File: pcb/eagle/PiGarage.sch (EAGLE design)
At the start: 19 parts, among them J1 JST_2PIN_HEADER, J2 JST_2PIN_HEADER, J3 JST_2PIN_HEADER, J4 RPI-GPIO-20X2, K1 G5LE, T1 NUD3105

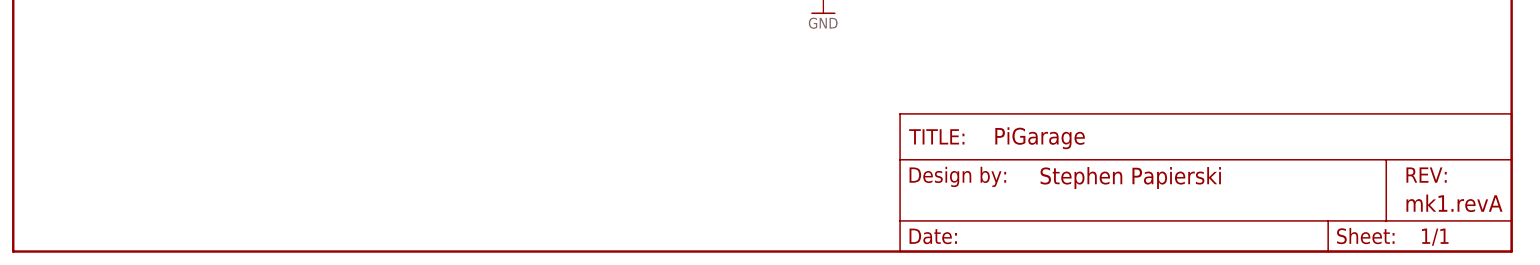
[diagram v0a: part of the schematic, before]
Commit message: Fixed relay NC/NO pin swap issue, bumped board rev to mk1.revB
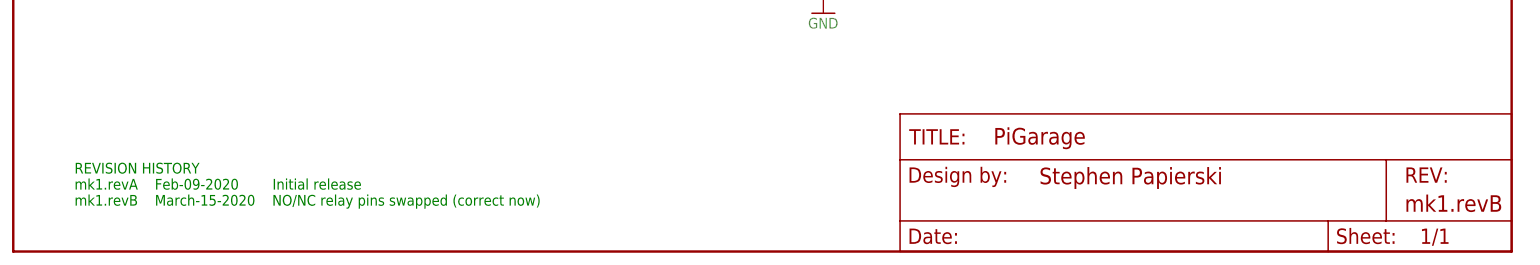
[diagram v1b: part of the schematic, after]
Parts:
- FRAME1: REV mk1.revA -> mk1.revB
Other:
- note added: "REVISION HISTORY mk1.revA Feb-09-2020 Initial release mk1.revB March-15-2020 NO/NC relay pins swapped (correct now)"
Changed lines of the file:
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@@
 <?xml version="1.0" encoding="utf-8"?>
 <!DOCTYPE eagle SYSTEM "eagle.dtd">
-<eagle version="9.2.0">
+<eagle version="9.5.2">
 <drawing>
 <settings>
-<setting alwaysvectorfont="yes"/>
+<setting alwaysvectorfont="no"/>
 <setting verticaltext="up"/>
 </settings>
@@
 <part name="FRAME1" library="eagle_stephen_v1.1" deviceset="FRAME-LETTER" device="NO_PACKAGE">
 <attribute name="DESIGNER" value="Stephen Papierski"/>
-<attribute name="REV" value="mk1.revA"/>
+<attribute name="REV" value="mk1.revB"/>
 </part>
 </parts>
@@
 <text x="-15.24" y="-25.4" size="1.778" layer="97">DOOR_OPEN</text>
 <text x="132.04" y="-23.92" size="1.778" layer="97" rot="R180">DOOR_CTRL</text>
+<text x="-96.52" y="-116.84" size="1.778" layer="91">REVISION HISTORY
+mk1.revA    Feb-09-2020        Initial release
+mk1.revB    March-15-2020    NO/NC relay pins swapped (correct now)</text>
 </plain>
 <instances>
-<instance part="K1" gate="1" x="66" y="-34.08">
+<instance part="K1" gate="1" x="66" y="-34.08" smashed="yes">
 <attribute name="VALUE" x="67.27" y="-31.159" size="1.778" layer="96"/>
 <attribute name="PART" x="67.27" y="-29" size="1.778" layer="95"/>
 </instance>
-<instance part="K1" gate="2" x="88.86" y="-34.08">
+<instance part="K1" gate="2" x="88.86" y="-34.08" smashed="yes">
 <attribute name="PART" x="91.4" y="-34.08" size="1.778" layer="95"/>
 </instance>
-<instance part="GND5" gate="1" x="66" y="-69.64">
+<instance part="GND5" gate="1" x="66" y="-69.64" smashed="yes">
 <attribute name="VALUE" x="63.46" y="-72.18" size="1.778" layer="96"/>
 </instance>
-<instance part="J4" gate="G$1" x="55.88" y="12.7">
+<instance part="J4" gate="G$1" x="55.88" y="12.7" smashed="yes">
 <attribute name="VALUE" x="52.07" y="-17.526" size="1.778" layer="96" font="vector"/>
 <attribute name="NAME" x="52.07" y="38.608" size="1.778" layer="95" font="vector"/>
 </instance>
-<instance part="R5" gate="G$1" x="12.7" y="-25.4" rot="R90">
+<instance part="R5" gate="G$1" x="12.7" y="-25.4" smashed="yes" rot="R90">
 <attribute name="NAME" x="11.176" y="-25.4" size="1.778" layer="95" font="vector" rot="R90" align="bottom-center"/>
 <attribute name="VALUE" x="14.224" y="-25.4" size="1.778" layer="96" font="vector" rot="R90" align="top-center"/>
 </instance>
-<instance part="R4" gate="G$1" x="7.62" y="-10.16" rot="R90">
+<instance part="R4" gate="G$1" x="7.62" y="-10.16" smashed="yes" rot="R90">
 <attribute name="NAME" x="6.096" y="-10.16" size="1.778" layer="95" font="vector" rot="R90" align="bottom-center"/>
 <attribute name="VALUE" x="9.144" y="-10.16" size="1.778" layer="96" font="vector" rot="R90" align="top-center"/>
 </instance>
-<instance part="GND2" gate="1" x="12.7" y="-38.1">
+<instance part="GND2" gate="1" x="12.7" y="-38.1" smashed="yes">
 <attribute name="VALUE" x="10.16" y="-40.64" size="1.778" layer="96"/>
 </instance>
-<instance part="P+3" gate="1" x="66" y="-18.84">
+<instance part="P+3" gate="1" x="66" y="-18.84" smashed="yes">
 <attribute name="VALUE" x="63.46" y="-23.92" size="1.778" layer="96" rot="R90"/>
 </instance>
-<instance part="+3V31" gate="G$1" x="2.54" y="12.7">
+<instance part="+3V31" gate="G$1" x="2.54" y="12.7" smashed="yes">
 <attribute name="VALUE" x="0" y="7.62" size="1.778" layer="96" rot="R90"/>
 </instance>
-<instance part="LED3" gate="G$1" x="-45.72" y="5.08">
+<instance part="LED3" gate="G$1" x="-45.72" y="5.08" smashed="yes">
 <attribute name="NAME" x="-42.164" y="0.508" size="1.778" layer="95" rot="R90"/>
 <attribute name="VALUE" x="-40.005" y="0.508" size="1.778" layer="96" rot="R90"/>
 </instance>
-<instance part="LED2" gate="G$1" x="-60.96" y="5.08">
+<instance part="LED2" gate="G$1" x="-60.96" y="5.08" smashed="yes">
 <attribute name="NAME" x="-57.404" y="0.508" size="1.778" layer="95" rot="R90"/>
 <attribute name="VALUE" x="-55.245" y="0.508" size="1.778" layer="96" rot="R90"/>
 </instance>
-<instance part="LED1" gate="G$1" x="-76.2" y="5.08">
+<instance part="LED1" gate="G$1" x="-76.2" y="5.08" smashed="yes">
 <attribute name="NAME" x="-72.644" y="0.508" size="1.778" layer="95" rot="R90"/>
 <attribute name="VALUE" x="-70.485" y="0.508" size="1.778" layer="96" rot="R90"/>
 </instance>
-<instance part="LED4" gate="G$1" x="-91.44" y="5.08">
+<instance part="LED4" gate="G$1" x="-91.44" y="5.08" smashed="yes">
 <attribute name="NAME" x="-87.884" y="0.508" size="1.778" layer="95" rot="R90"/>
 <attribute name="VALUE" x="-85.725" y="0.508" size="1.778" layer="96" rot="R90"/>
 </instance>
-<instance part="R3" gate="G$1" x="-45.72" y="-7.62" rot="R90">
+<instance part="R3" gate="G$1" x="-45.72" y="-7.62" smashed="yes" rot="R90">
 <attribute name="NAME" x="-47.244" y="-7.62" size="1.778" layer="95" font="vector" rot="R90" align="bottom-center"/>
 <attribute name="VALUE" x="-44.196" y="-7.62" size="1.778" layer="96" font="vector" rot="R90" align="top-center"/>
 </instance>
-<instance part="R2" gate="G$1" x="-60.96" y="-7.62" rot="R90">
+<instance part="R2" gate="G$1" x="-60.96" y="-7.62" smashed="yes" rot="R90">
 <attribute name="NAME" x="-62.484" y="-7.62" size="1.778" layer="95" font="vector" rot="R90" align="bottom-center"/>
 <attribute name="VALUE" x="-59.436" y="-7.62" size="1.778" layer="96" font="vector" rot="R90" align="top-center"/>
 </instance>
-<instance part="R1" gate="G$1" x="-76.2" y="-7.62" rot="R90">
+<instance part="R1" gate="G$1" x="-76.2" y="-7.62" smashed="yes" rot="R90">
 <attribute name="NAME" x="-77.724" y="-7.62" size="1.778" layer="95" font="vector" rot="R90" align="bottom-center"/>
 <attribute name="VALUE" x="-74.676" y="-7.62" size="1.778" layer="96" font="vector" rot="R90" align="top-center"/>
 </instance>
-<instance part="R6" gate="G$1" x="-91.44" y="-7.62" rot="R90">
+<instance part="R6" gate="G$1" x="-91.44" y="-7.62" smashed="yes" rot="R90">
 <attribute name="NAME" x="-92.964" y="-7.62" size="1.778" layer="95" font="vector" rot="R90" align="bottom-center"/>
 <attribute name="VALUE" x="-89.916" y="-7.62" size="1.778" layer="96" font="vector" rot="R90" align="top-center"/>
 </instance>
-<instance part="GND1" gate="1" x="-60.96" y="-20.32">
+<instance part="GND1" gate="1" x="-60.96" y="-20.32" smashed="yes">
 <attribute name="VALUE" x="-63.5" y="-22.86" size="1.778" layer="96"/>
 </instance>
-<instance part="T1" gate="G$1" x="63.46" y="-54.4">
+<instance part="T1" gate="G$1" x="63.46" y="-54.4" smashed="yes">
 <attribute name="NAME" x="71.08" y="-54.4" size="1.778" layer="95" font="vector"/>
 <attribute name="VALUE" x="71.08" y="-56.94" size="1.778" layer="96" font="vector"/>
 </instance>
-<instance part="P+1" gate="1" x="-91.44" y="12.7">
+<instance part="P+1" gate="1" x="-91.44" y="12.7" smashed="yes">
 <attribute name="VALUE" x="-93.98" y="7.62" size="1.778" layer="96" rot="R90"/>
 </instance>
-<instance part="GND3" gate="1" x="-91.44" y="-20.32">
+<instance part="GND3" gate="1" x="-91.44" y="-20.32" smashed="yes">
 <attribute name="VALUE" x="-93.98" y="-22.86" size="1.778" layer="96"/>
 </instance>
-<instance part="J1" gate="&gt;NAME" x="-12.7" y="2.54">
+<instance part="J1" gate="&gt;NAME" x="-12.7" y="2.54" smashed="yes">
 <attribute name="VALUE" x="-15.24" y="-2.54" size="1.778" layer="96"/>
 <attribute name="NAME" x="-15.24" y="8.382" size="1.778" layer="95"/>
 </instance>
-<instance part="J2" gate="&gt;NAME" x="-12.7" y="-17.78">
+<instance part="J2" gate="&gt;NAME" x="-12.7" y="-17.78" smashed="yes">
 <attribute name="VALUE" x="-15.24" y="-22.86" size="1.778" layer="96"/>
 <attribute name="NAME" x="-15.24" y="-11.938" size="1.778" layer="95"/>
 </instance>
-<instance part="J3" gate="&gt;NAME" x="129.5" y="-31.54" rot="R180">
+<instance part="J3" gate="&gt;NAME" x="129.5" y="-31.54" smashed="yes" rot="R180">
 <attribute name="VALUE" x="132.04" y="-26.46" size="1.778" layer="96" rot="R180"/>
 <attribute name="NAME" x="132.04" y="-37.382" size="1.778" layer="95" rot="R180"/>
 </instance>
-<instance part="LED5" gate="G$1" x="27.9" y="-62.02">
+<instance part="LED5" gate="G$1" x="27.9" y="-62.02" smashed="yes">
 <attribute name="NAME" x="31.456" y="-66.592" size="1.778" layer="95" rot="R90"/>
 <attribute name="VALUE" x="33.615" y="-66.592" size="1.778" layer="96" rot="R90"/>
 </instance>
-<instance part="R7" gate="G$1" x="27.9" y="-74.72" rot="R90">
+<instance part="R7" gate="G$1" x="27.9" y="-74.72" smashed="yes" rot="R90">
 <attribute name="NAME" x="26.376" y="-74.72" size="1.778" layer="95" font="vector" rot="R90" align="bottom-center"/>
 <attribute name="VALUE" x="29.424" y="-74.72" size="1.778" layer="96" font="vector" rot="R90" align="top-center"/>
 </instance>
-<instance part="GND4" gate="1" x="27.9" y="-84.88">
+<instance part="GND4" gate="1" x="27.9" y="-84.88" smashed="yes">
 <attribute name="VALUE" x="25.36" y="-87.42" size="1.778" layer="96"/>
 </instance>
-<instance part="FRAME1" gate="G$1" x="-106.68" y="-124.46"/>
-<instance part="FRAME1" gate="V" x="40.64" y="-124.46">
+<instance part="FRAME1" gate="G$1" x="-106.68" y="-124.46" smashed="yes"/>
+<instance part="FRAME1" gate="V" x="40.64" y="-124.46" smashed="yes">
 <attribute name="LAST_DATE_TIME" x="53.34" y="-123.19" size="2.54" layer="94" font="vector"/>
 <attribute name="SHEET" x="127" y="-123.19" size="2.54" layer="94" font="vector"/>
@@
 </drawing>
 <compatibility>
+<note version="6.3" minversion="6.2.2" severity="warning">
+Since Version 6.2.2 text objects can contain more than one line,
+which will not be processed correctly with this version.
+</note>
 <note version="8.2" severity="warning">
 Since Version 8.2, EAGLE supports online libraries. The ids
